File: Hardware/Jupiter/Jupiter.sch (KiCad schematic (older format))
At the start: 118 parts

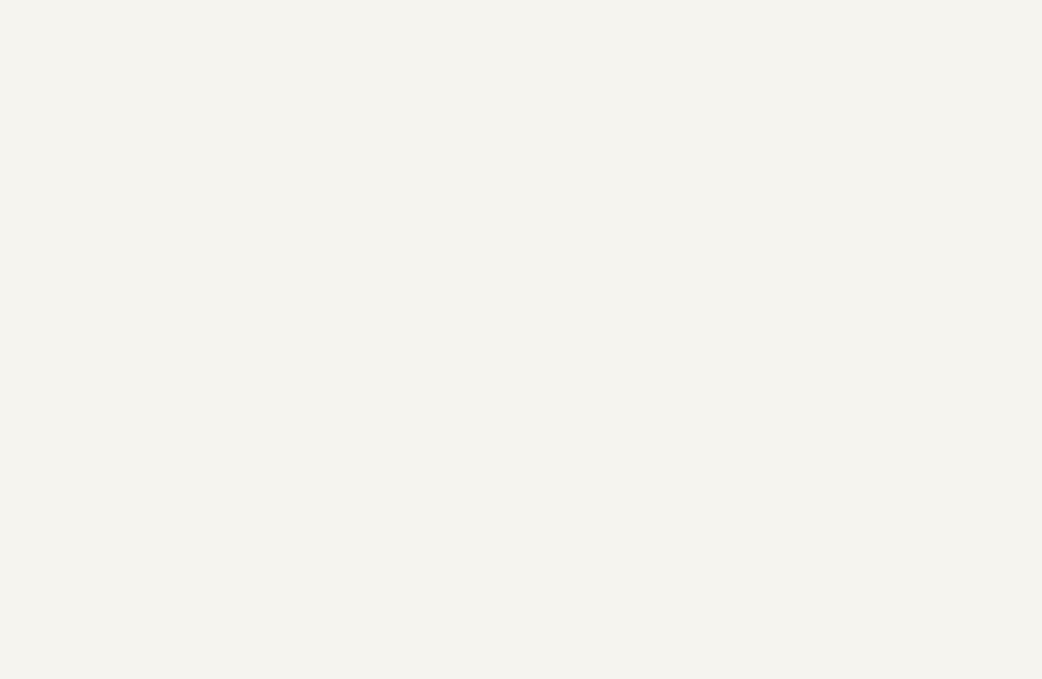
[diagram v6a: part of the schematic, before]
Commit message: Add SD card slot.
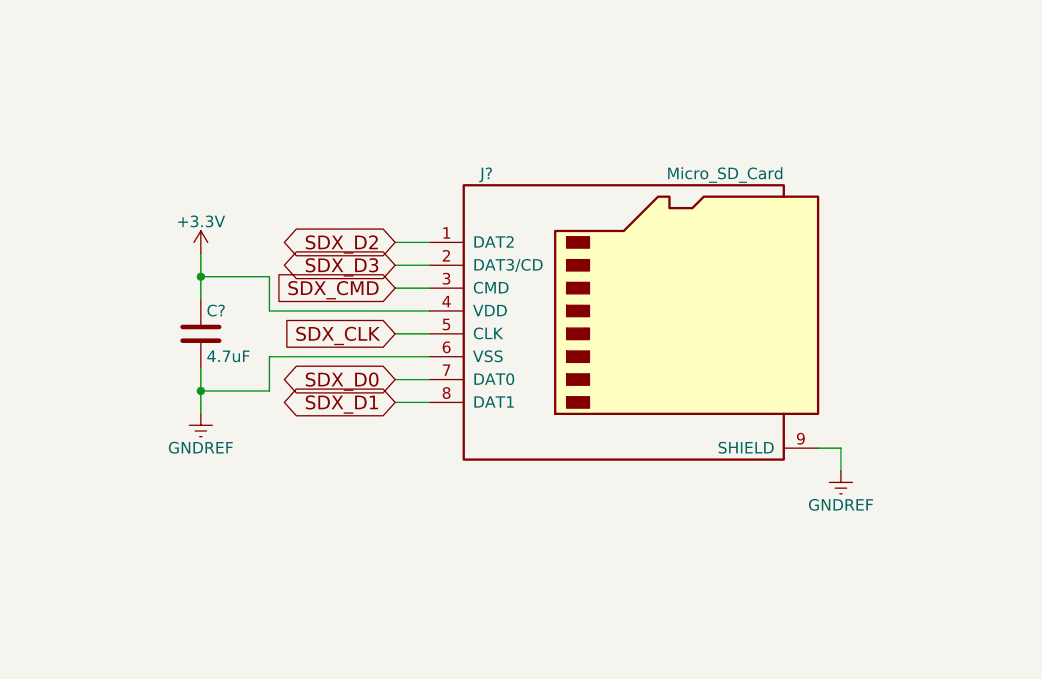
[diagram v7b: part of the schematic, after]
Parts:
- added C?: 4.7uF, symbol C
- added J?: Micro_SD_Card, symbol Micro_SD_Card
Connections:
- net +3V3: now also C?.1, J?.4 (VDD)
- net GNDREF: now also C?.2, J?.6 (VSS), J?.9 (SHIELD)
- net SDX_CLK: now also J?.5 (CLK)
- net SDX_CMD: now also J?.3 (CMD)
- net SDX_D0: now also J?.7 (DAT0)
- net SDX_D1: now also J?.8 (DAT1)
- net SDX_D2: now also J?.1 (DAT2)
- net SDX_D3: now also J?.2 (DAT3/CD)
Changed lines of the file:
@@
 Wire Wire Line
 	2550 9300 2500 9300
+$Comp
+L Micro_SD_Card J?
+U 1 1 5B7952D0
+P 9350 6000
+F 0 "J?" H 8700 6600 50  0000 C CNN
+F 1 "Micro_SD_Card" H 10000 6600 50  0000 R CNN
+F 2 "" H 10500 6300 50  0001 C CNN
+F 3 "" H 9350 6000 50  0001 C CNN
+	1    9350 6000
+	1    0    0    -1
+$EndComp
+Text GLabel 8300 5700 0    60   BiDi ~ 0
+SDX_D2
+Text GLabel 8300 5800 0    60   BiDi ~ 0
+SDX_D3
+Text GLabel 8300 5900 0    60   Input ~ 0
+SDX_CMD
+Text GLabel 8300 6100 0    60   Input ~ 0
+SDX_CLK
+Text GLabel 8300 6300 0    60   BiDi ~ 0
+SDX_D0
+Text GLabel 8300 6400 0    60   BiDi ~ 0
+SDX_D1
+Wire Wire Line
+	8450 6400 8300 6400
+Wire Wire Line
+	8300 6300 8450 6300
+Wire Wire Line
+	8450 6100 8300 6100
+Wire Wire Line
+	8450 5900 8300 5900
+Wire Wire Line
+	8450 5800 8300 5800
+Wire Wire Line
+	8450 5700 8300 5700
+$Comp
+L C C?
+U 1 1 5B799037
+P 7450 6100
+F 0 "C?" H 7475 6200 50  0000 L CNN
+F 1 "4.7uF" H 7475 6000 50  0000 L CNN
+F 2 "" H 7488 5950 50  0001 C CNN
+F 3 "" H 7450 6100 50  0001 C CNN
+	1    7450 6100
+	1    0    0    -1
+$EndComp
+$Comp
+L GNDREF #PWR?
+U 1 1 5B7992B8
+P 7450 6450
+F 0 "#PWR?" H 7450 6200 50  0001 C CNN
+F 1 "GNDREF" H 7450 6300 50  0000 C CNN
+F 2 "" H 7450 6450 50  0001 C CNN
+F 3 "" H 7450 6450 50  0001 C CNN
+	1    7450 6450
+	1    0    0    -1
+$EndComp
+$Comp
+L +3.3V #PWR?
+U 1 1 5B7993BC
+P 7450 5750
+F 0 "#PWR?" H 7450 5600 50  0001 C CNN
+F 1 "+3.3V" H 7450 5890 50  0000 C CNN
+F 2 "" H 7450 5750 50  0001 C CNN
+F 3 "" H 7450 5750 50  0001 C CNN
+	1    7450 5750
+	1    0    0    -1
+$EndComp
+Wire Wire Line
+	7450 5750 7450 5950
+Wire Wire Line
+	7450 6250 7450 6450
+Wire Wire Line
+	8450 6000 7750 6000
+Wire Wire Line
+	7750 6000 7750 5850
+Wire Wire Line
+	7750 5850 7450 5850
+Connection ~ 7450 5850
+Wire Wire Line
+	8450 6200 7750 6200
+Wire Wire Line
+	7750 6200 7750 6350
+Wire Wire Line
+	7750 6350 7450 6350
+Connection ~ 7450 6350
+$Comp
+L GNDREF #PWR?
+U 1 1 5B79AC32
+P 10250 6700
+F 0 "#PWR?" H 10250 6450 50  0001 C CNN
+F 1 "GNDREF" H 10250 6550 50  0000 C CNN
+F 2 "" H 10250 6700 50  0001 C CNN
+F 3 "" H 10250 6700 50  0001 C CNN
+	1    10250 6700
+	1    0    0    -1
+$EndComp
+Wire Wire Line
+	10250 6700 10250 6600
+Wire Wire Line
+	10250 6600 10150 6600
 $EndSCHEMATC

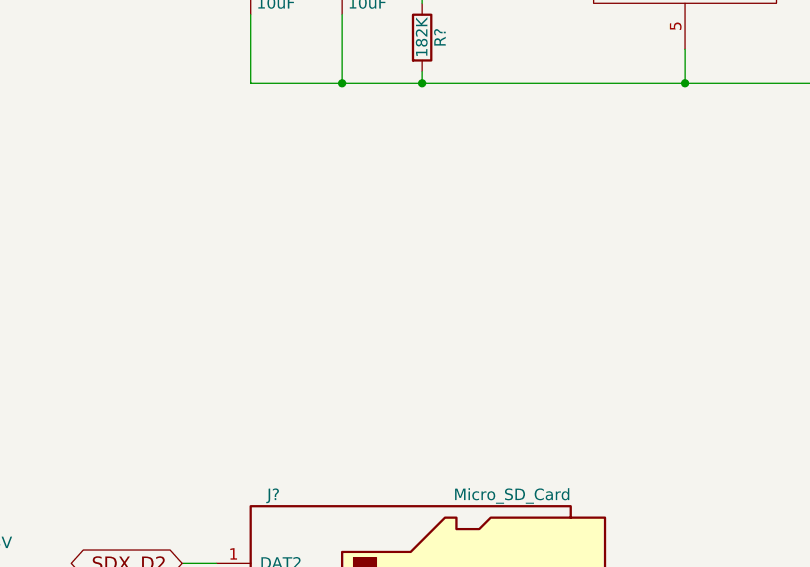
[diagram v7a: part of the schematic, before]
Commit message: Denote power flags and export schematic documentation.
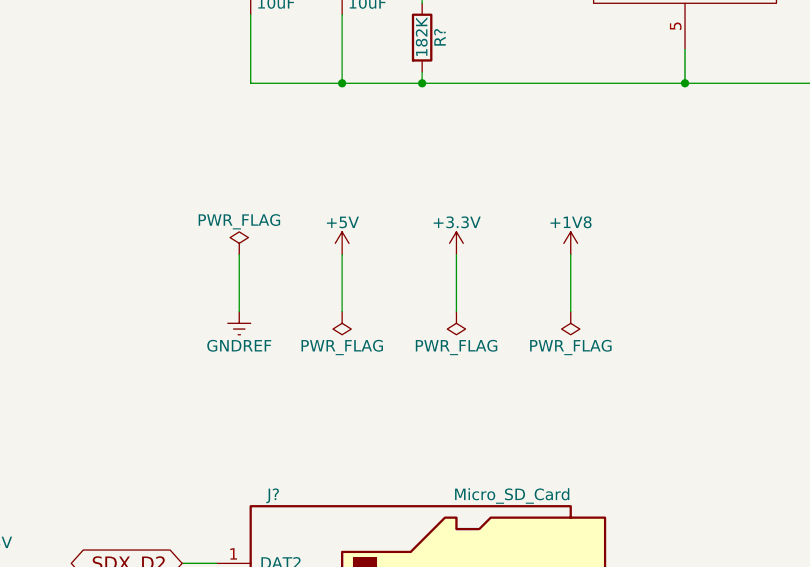
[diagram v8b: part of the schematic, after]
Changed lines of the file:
@@
 Wire Wire Line
 	10250 6600 10150 6600
+$Comp
+L PWR_FLAG #FLG?
+U 1 1 5B79E360
+P 8550 4350
+F 0 "#FLG?" H 8550 4425 50  0001 C CNN
+F 1 "PWR_FLAG" H 8550 4500 50  0000 C CNN
+F 2 "" H 8550 4350 50  0001 C CNN
+F 3 "" H 8550 4350 50  0001 C CNN
+	1    8550 4350
+	1    0    0    -1
+$EndComp
+$Comp
+L PWR_FLAG #FLG?
+U 1 1 5B79E464
+P 9000 4600
+F 0 "#FLG?" H 9000 4675 50  0001 C CNN
+F 1 "PWR_FLAG" H 9000 4750 50  0000 C CNN
+F 2 "" H 9000 4600 50  0001 C CNN
+F 3 "" H 9000 4600 50  0001 C CNN
+	1    9000 4600
+	-1   0    0    1
+$EndComp
+$Comp
+L PWR_FLAG #FLG?
+U 1 1 5B79E8BC
+P 9500 4600
+F 0 "#FLG?" H 9500 4675 50  0001 C CNN
+F 1 "PWR_FLAG" H 9500 4750 50  0000 C CNN
+F 2 "" H 9500 4600 50  0001 C CNN
+F 3 "" H 9500 4600 50  0001 C CNN
+	1    9500 4600
+	-1   0    0    1
+$EndComp
+$Comp
+L GNDREF #PWR?
+U 1 1 5B79ED8C
+P 8550 4600
+F 0 "#PWR?" H 8550 4350 50  0001 C CNN
+F 1 "GNDREF" H 8550 4450 50  0000 C CNN
+F 2 "" H 8550 4600 50  0001 C CNN
+F 3 "" H 8550 4600 50  0001 C CNN
+	1    8550 4600
+	1    0    0    -1
+$EndComp
+Wire Wire Line
+	8550 4600 8550 4350
+$Comp
+L PWR_FLAG #FLG?
+U 1 1 5B79F6EC
+P 10000 4600
+F 0 "#FLG?" H 10000 4675 50  0001 C CNN
+F 1 "PWR_FLAG" H 10000 4750 50  0000 C CNN
+F 2 "" H 10000 4600 50  0001 C CNN
+F 3 "" H 10000 4600 50  0001 C CNN
+	1    10000 4600
+	-1   0    0    1
+$EndComp
+$Comp
+L +5V #PWR?
+U 1 1 5B79FB4E
+P 9000 4350
+F 0 "#PWR?" H 9000 4200 50  0001 C CNN
+F 1 "+5V" H 9000 4490 50  0000 C CNN
+F 2 "" H 9000 4350 50  0001 C CNN
+F 3 "" H 9000 4350 50  0001 C CNN
+	1    9000 4350
+	1    0    0    -1
+$EndComp
+$Comp
+L +3.3V #PWR?
+U 1 1 5B79FC52
+P 9500 4350
+F 0 "#PWR?" H 9500 4200 50  0001 C CNN
+F 1 "+3.3V" H 9500 4490 50  0000 C CNN
+F 2 "" H 9500 4350 50  0001 C CNN
+F 3 "" H 9500 4350 50  0001 C CNN
+	1    9500 4350
+	1    0    0    -1
+$EndComp
+$Comp
+L +1V8 #PWR?
+U 1 1 5B79FD56
+P 10000 4350
+F 0 "#PWR?" H 10000 4200 50  0001 C CNN
+F 1 "+1V8" H 10000 4490 50  0000 C CNN
+F 2 "" H 10000 4350 50  0001 C CNN
+F 3 "" H 10000 4350 50  0001 C CNN
+	1    10000 4350
+	1    0    0    -1
+$EndComp
+Wire Wire Line
+	10000 4350 10000 4600
+Wire Wire Line
+	9500 4350 9500 4600
+Wire Wire Line
+	9000 4350 9000 4600
 $EndSCHEMATC
